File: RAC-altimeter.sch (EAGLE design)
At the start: 33 parts, among them J1 MICRO-SD, J2 CORTEX_DEBUG_SMD, J3 282834-2, J4 JUMPER-SMT_2_NO_SILK, U1 MAX32660GTP+, U2 BMI088, U3 BMP388, U4 RN4871-I_RM130, U5 MCP1640T-I_CHY, Y1 32.768kHz

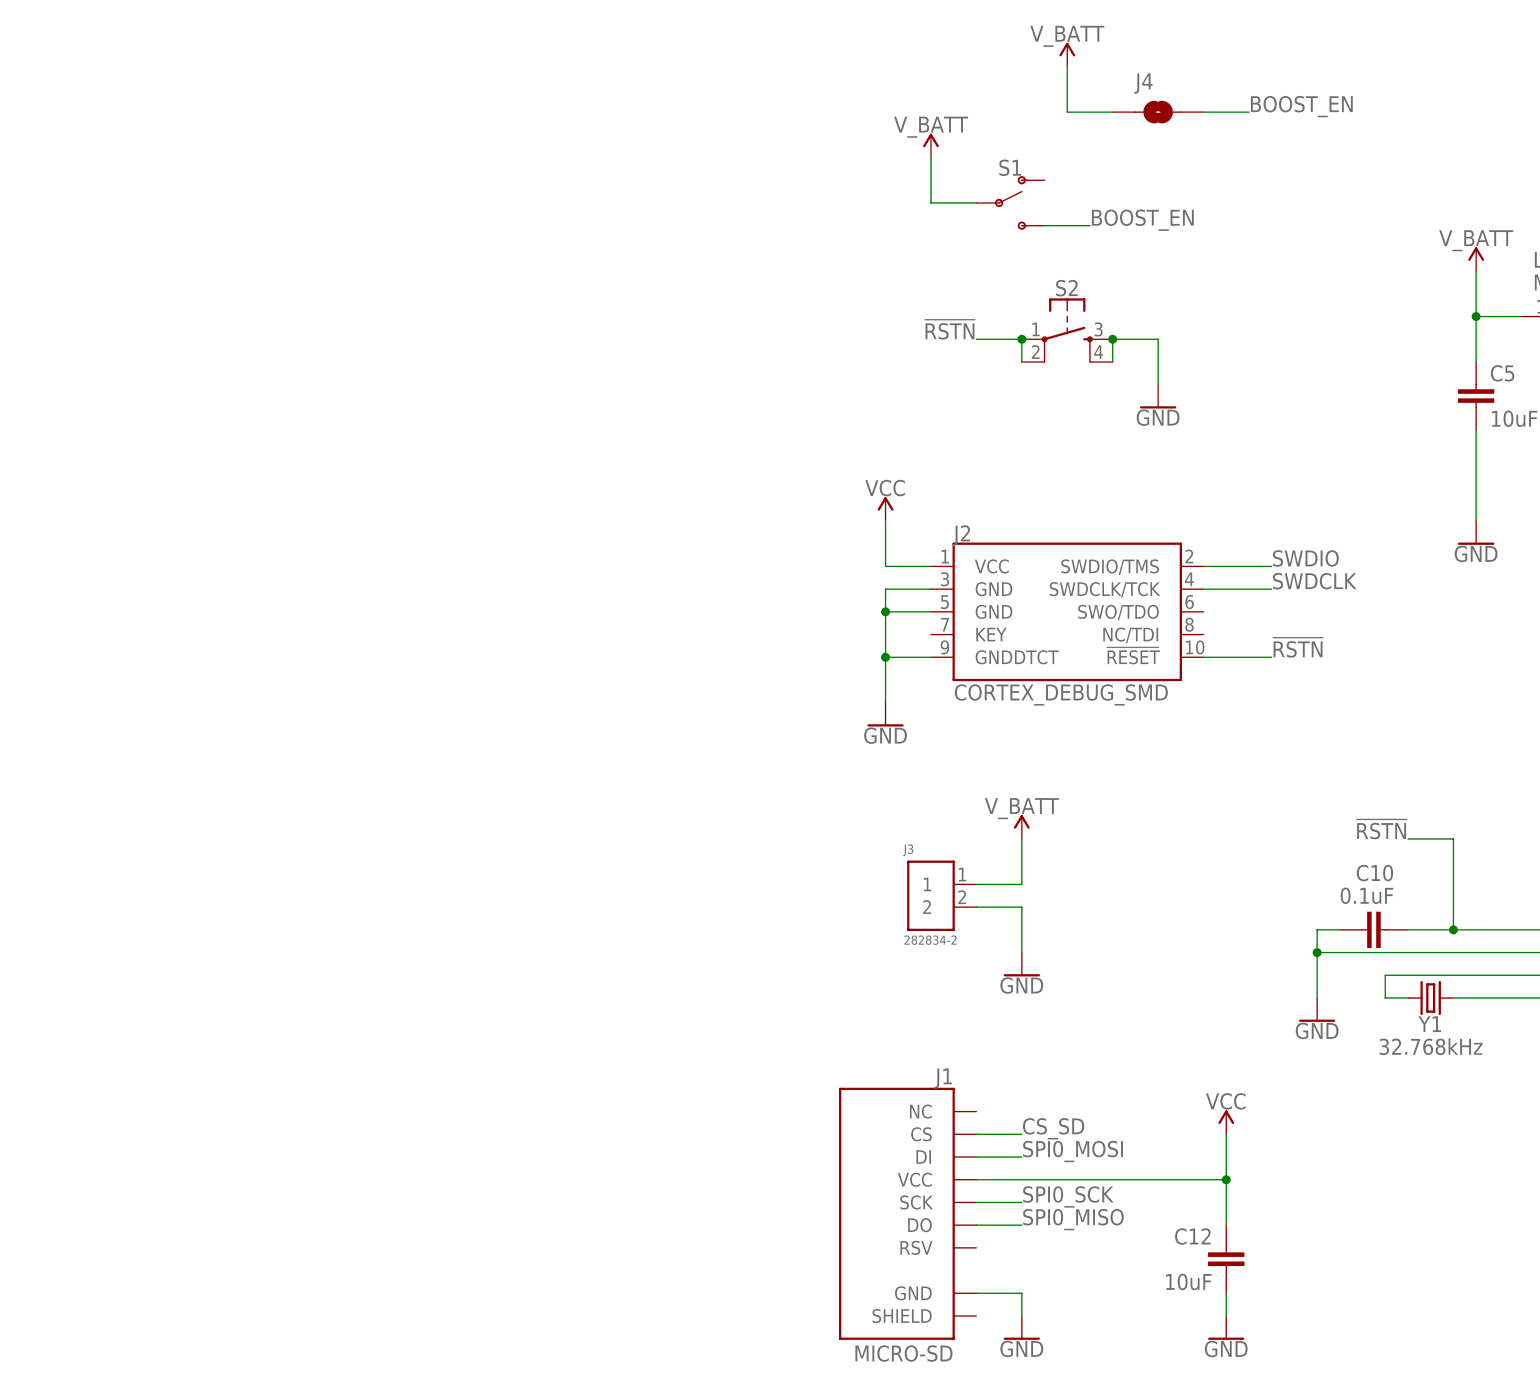
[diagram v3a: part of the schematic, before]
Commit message: Cleaned up the schematic arrangement
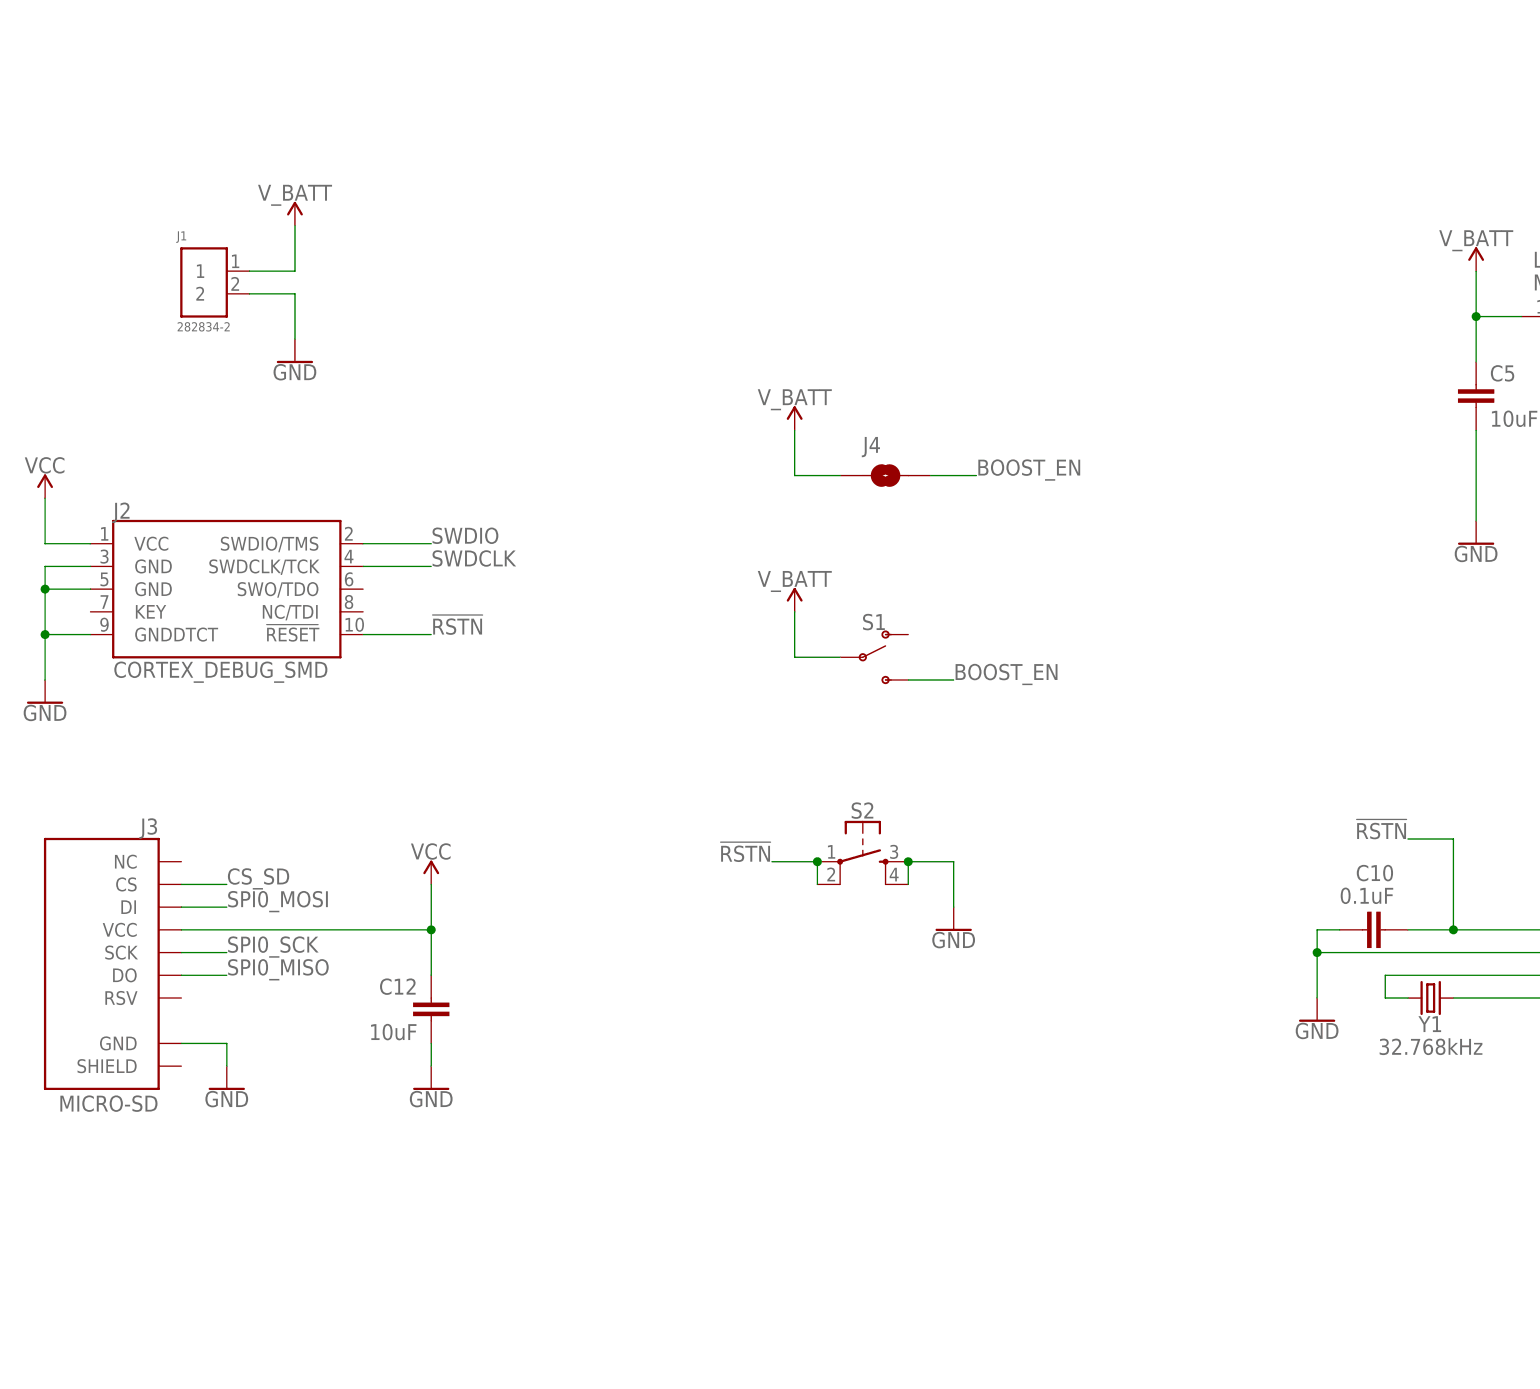
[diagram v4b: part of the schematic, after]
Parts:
- J1: value MICRO-SD -> 282834-2; device SparkFun-Connectors:MICRO-SD_CARD_SOCKETTINY -> RAC-Altimeter:282834-2
- J3: value 282834-2 -> MICRO-SD; device RAC-Altimeter:282834-2 -> SparkFun-Connectors:MICRO-SD_CARD_SOCKETTINY
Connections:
- net CS_SD: now also J3.CS; no longer J1.CS
- net GND: now also J1.2, J3.GND; no longer J1.GND, J3.2
- net SPI0_MISO: now also J3.DO; no longer J1.DO
- net SPI0_MOSI: now also J3.DI; no longer J1.DI
- net SPI0_SCK: now also J3.SCK; no longer J1.SCK
- net VCC: now also J3.VCC; no longer J1.VCC
- net V_BATT: now also J1.1; no longer J3.1
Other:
- moved on the sheet: C12, J2, J4, S1, S2

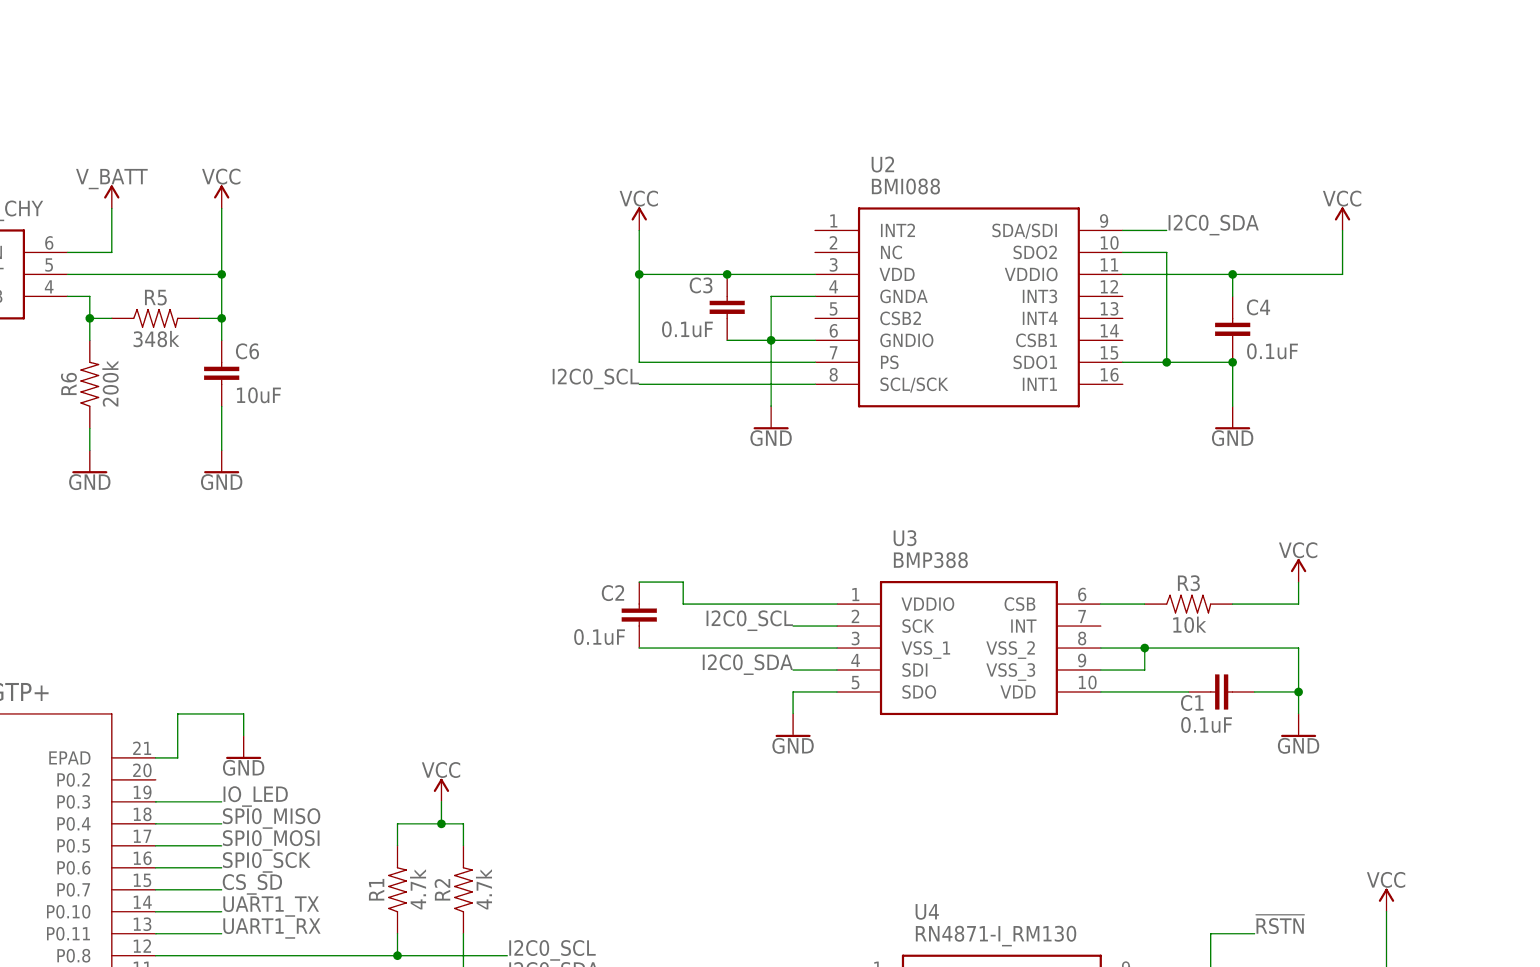
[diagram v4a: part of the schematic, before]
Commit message: Fixed net connections and routed IC groups
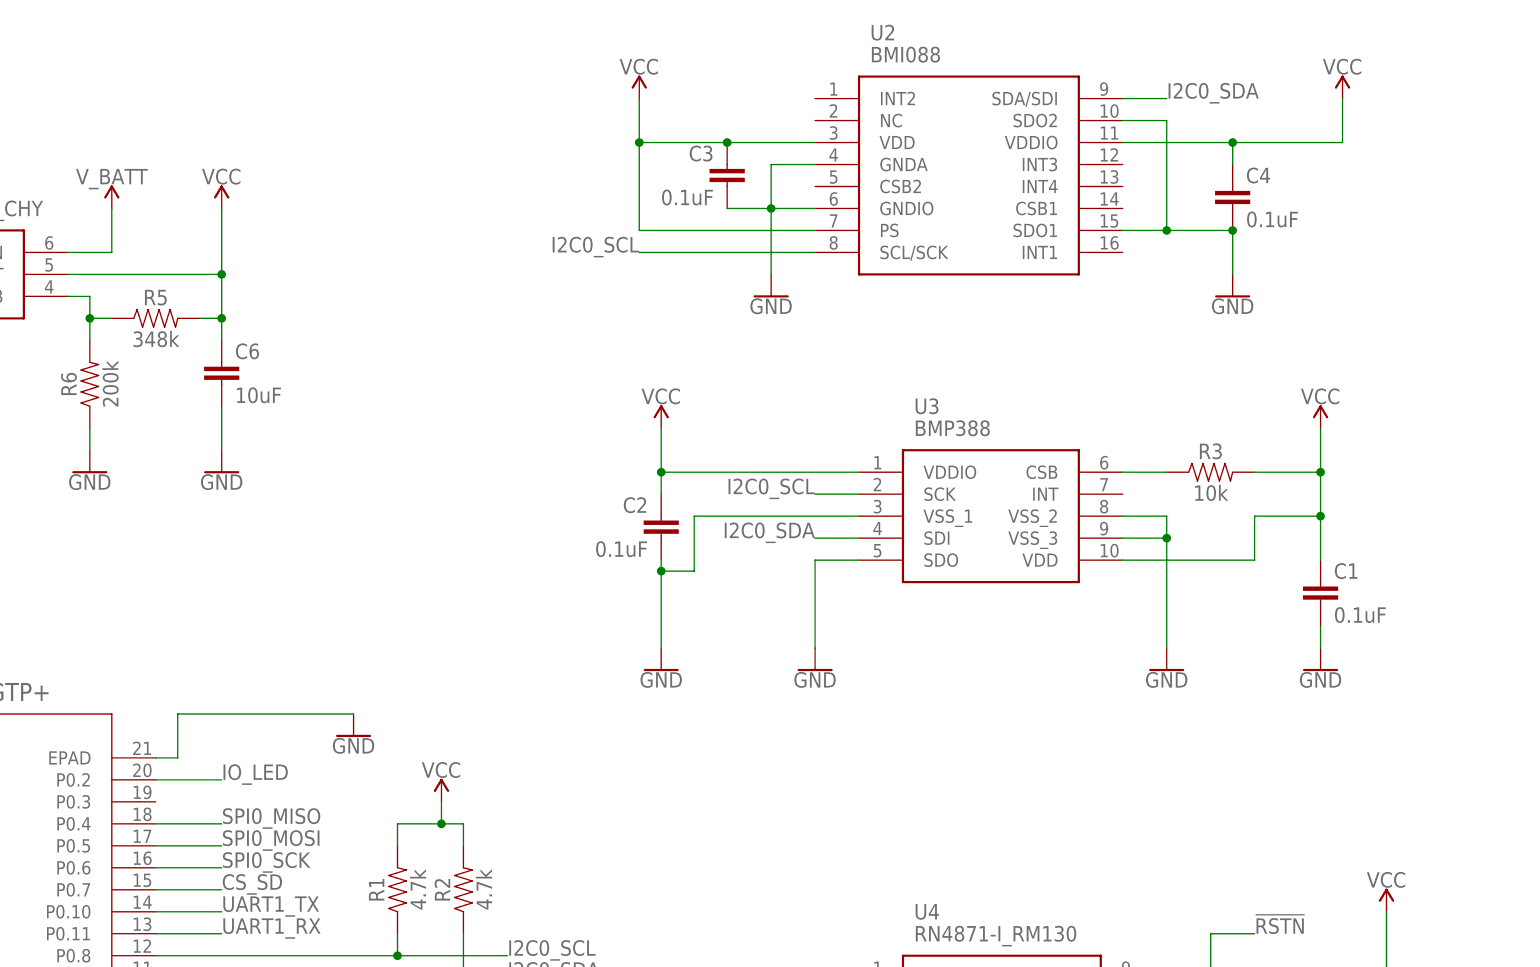
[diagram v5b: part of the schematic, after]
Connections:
- net N$10 renamed 32KOUT
- net N$11 renamed VCORE
- net N$2 renamed SW
- net N$3 renamed VFB
- net N$9 renamed 32KIN
- removed net N$4: C1.2, U3.VDD
- removed net N$5: C2.1, U3.VDDIO
- removed net N$6: C2.2, U3.VSS_1
- net GND: now also C1.2, C2.2, U3.VSS_1; no longer C1.1
- net IO_LED: now also U1.P0.2; no longer U1.P0.3
- net VCC: now also C1.1, C2.1, U3.VDD, U3.VDDIO
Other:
- moved on the sheet: C1, C2, C3, C4, R3, U2, U3

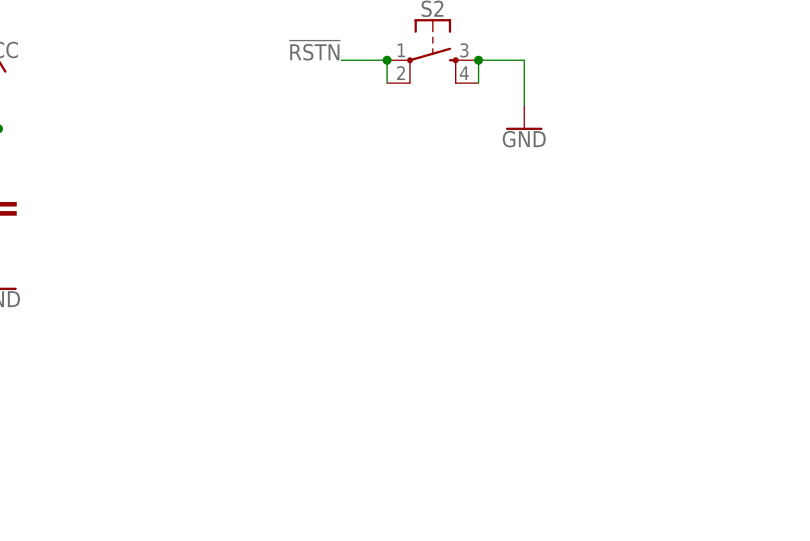
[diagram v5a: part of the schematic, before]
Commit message: Added PCB mounting holes
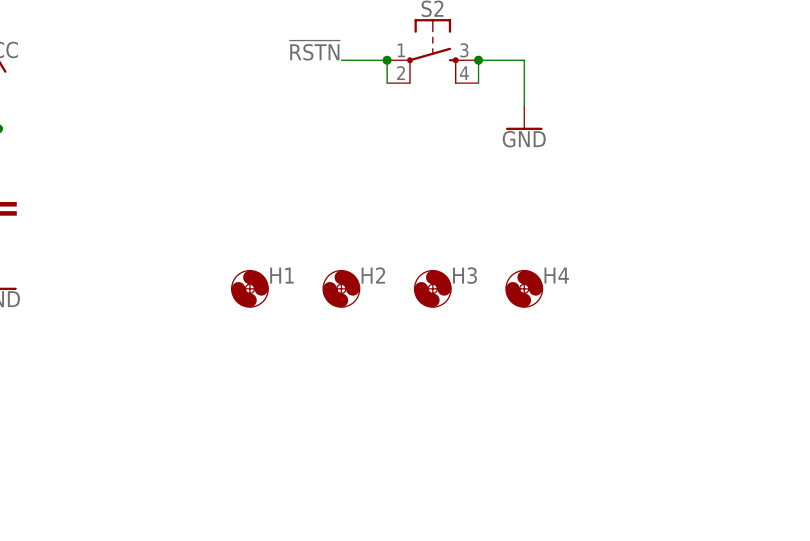
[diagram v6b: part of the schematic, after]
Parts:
- added H1, H2, H3, H4: MOUNT-HOLE2.8, holes:MOUNT-HOLE2.8
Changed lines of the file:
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@@
 <part name="C1" library="SparkFun-Capacitors" deviceset="0.1UF" device="-0603-25V-(+80/-20%)" value="0.1uF"/>
 <part name="GND22" library="SparkFun-PowerSymbols" deviceset="GND" device=""/>
+<part name="H1" library="holes" library_urn="urn:adsk.eagle:library:237" deviceset="MOUNT-HOLE" device="2.8" package3d_urn="urn:adsk.eagle:package:14271/1"/>
+<part name="H2" library="holes" library_urn="urn:adsk.eagle:library:237" deviceset="MOUNT-HOLE" device="2.8" package3d_urn="urn:adsk.eagle:package:14271/1"/>
+<part name="H3" library="holes" library_urn="urn:adsk.eagle:library:237" deviceset="MOUNT-HOLE" device="2.8" package3d_urn="urn:adsk.eagle:package:14271/1"/>
+<part name="H4" library="holes" library_urn="urn:adsk.eagle:library:237" deviceset="MOUNT-HOLE" device="2.8" package3d_urn="urn:adsk.eagle:package:14271/1"/>
 </parts>
 <sheets>
@@
 <attribute name="VALUE" x="172.72" y="70.866" size="1.778" layer="96" align="top-center"/>
 </instance>
+<instance part="H1" gate="G$1" x="-106.68" y="33.02" smashed="yes">
+<attribute name="NAME" x="-104.648" y="33.6042" size="1.778" layer="95"/>
+</instance>
+<instance part="H2" gate="G$1" x="-96.52" y="33.02" smashed="yes">
+<attribute name="NAME" x="-94.488" y="33.6042" size="1.778" layer="95"/>
+</instance>
+<instance part="H3" gate="G$1" x="-86.36" y="33.02" smashed="yes">
+<attribute name="NAME" x="-84.328" y="33.6042" size="1.778" layer="95"/>
+</instance>
+<instance part="H4" gate="G$1" x="-76.2" y="33.02" smashed="yes">
+<attribute name="NAME" x="-74.168" y="33.6042" size="1.778" layer="95"/>
+</instance>
 </instances>
